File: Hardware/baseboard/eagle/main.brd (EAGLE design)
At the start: 359.1 x 113.3 mm, 182 parts, among them J1 MICROUSB-FEM, X1 JST-4POS-2X4POS, X1.2 TACH/LAP, X2 ATLAS-LTC, X2.1 MOTOR, X2.2 VRAILS+, X2.3 5V+SoC, X5 15244441

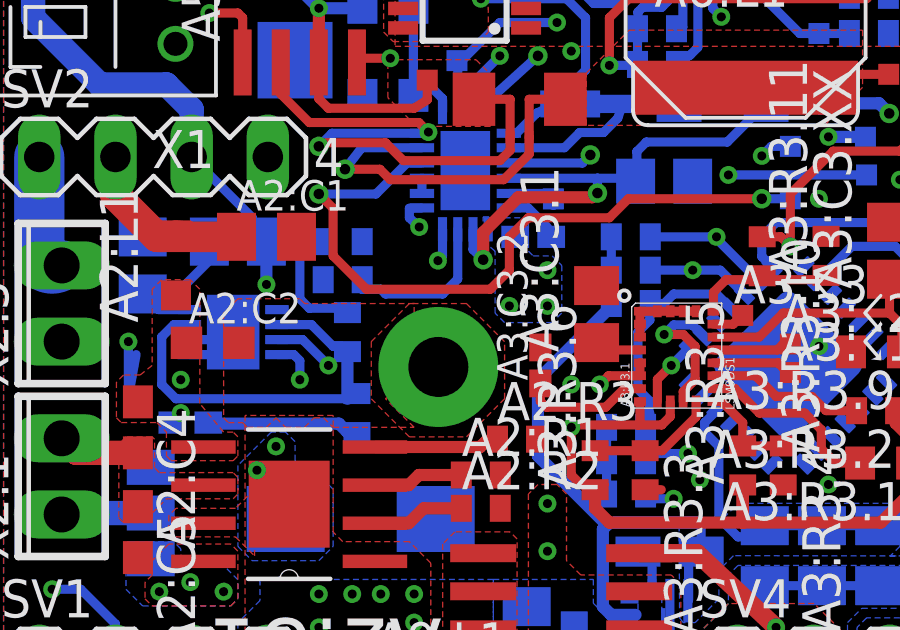
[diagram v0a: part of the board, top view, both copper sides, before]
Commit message: wip baseboard  -> layout: did some easy airwires
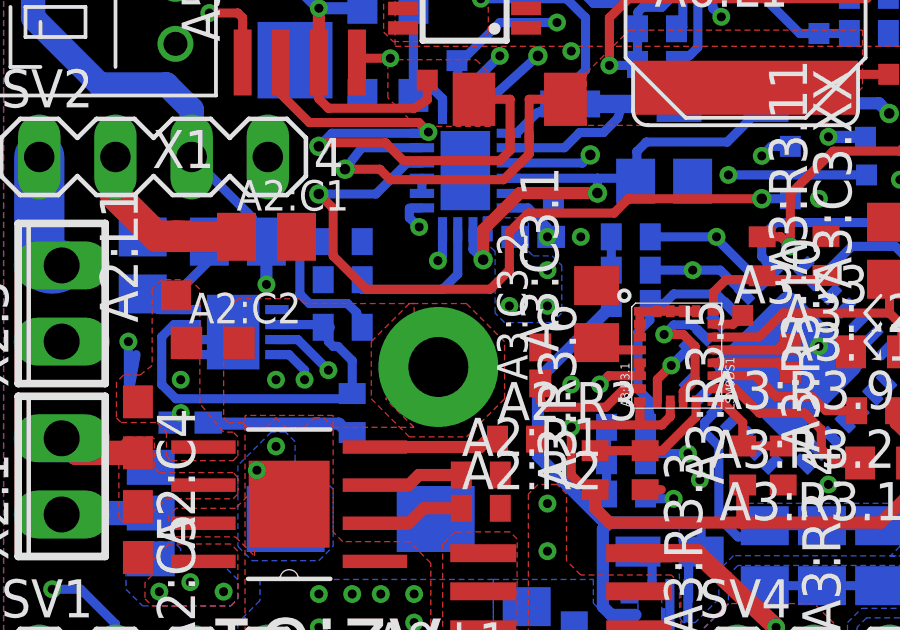
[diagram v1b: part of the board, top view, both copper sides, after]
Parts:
- moved A10:R2 0.22 mm to (17.3, 30.3), turned to 180 degrees
- moved A10:R1 0.16 mm to (17.6, 27.5)
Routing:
- net A10:HYST: track 4.38 -> 5.12 mm
- net GND: vias 40 -> 43

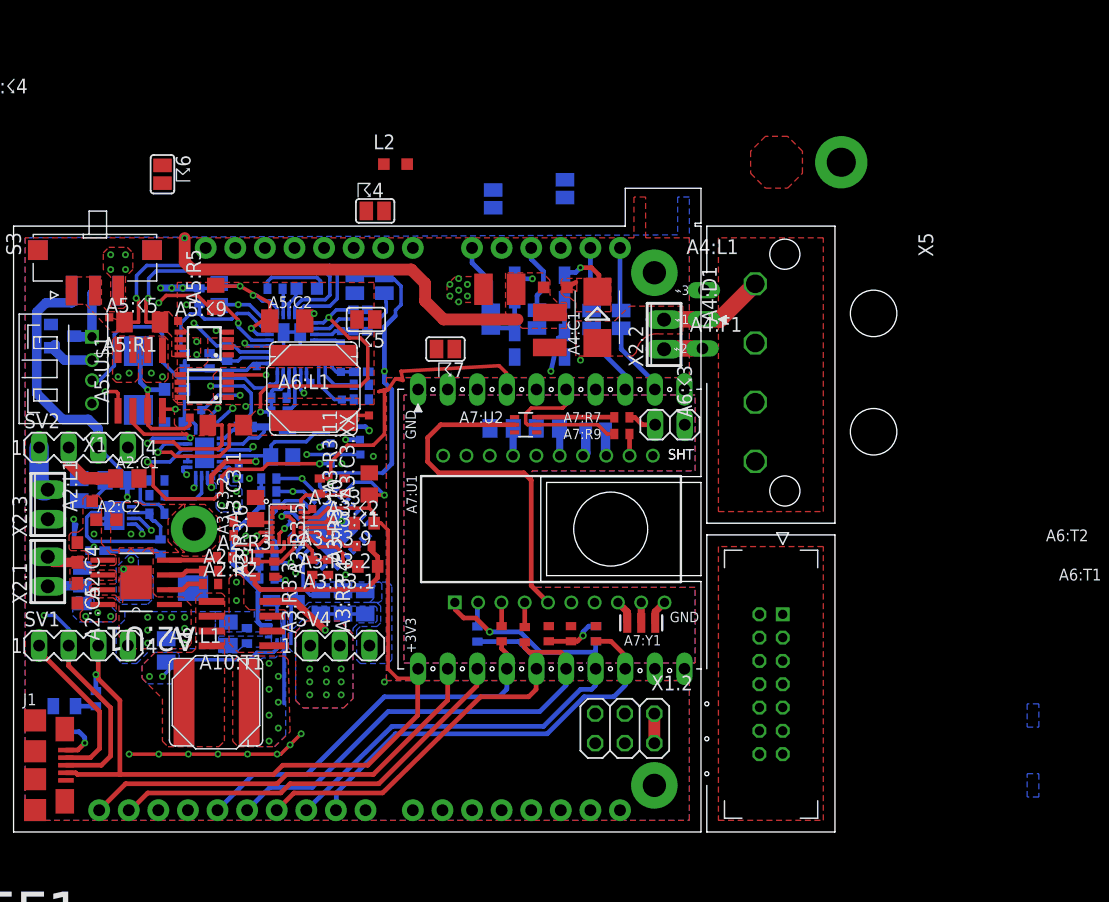
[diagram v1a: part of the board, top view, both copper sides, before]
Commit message: wip baseboard layout quicksave  + schematic    -> revised high side guard, added NAND logic  + layout    -> moved entire guard circuit on north west corner,       ideal fit acutally. Spooky how this works.    -> redo of input protection and powerlines,       make slightly more sense now
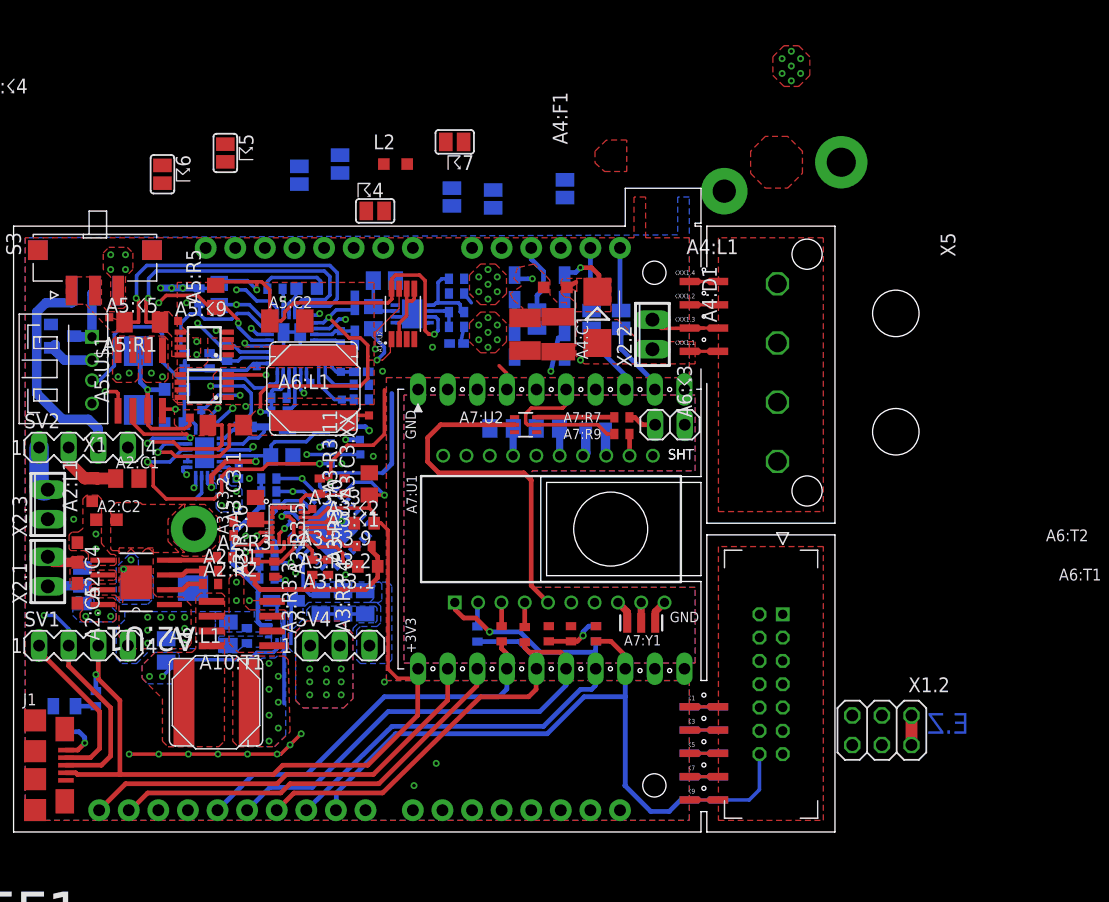
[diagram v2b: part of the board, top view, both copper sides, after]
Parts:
- removed ⌁1: SINGLEPAD40MIL-BREAK.PILOT, kitt.con:PAD40MIL.BREAK_PILOT
- removed ⌁2, ⌁3: SINGLEPAD40MIL-BREAK, kitt.con:PAD40MIL.BREAK
- added A10:U2: 2NANDSOP8, kitt.ic:SOP65P490X110-8N
- added ☇1: 1, kitt.con:CON.BUOC.BREAKPAD-P5MM
- added ☇10: 10, kitt.con:CON.BUOC.BREAKPAD-P5MM
- added ☇2: 2, kitt.con:CON.BUOC.BREAKPAD-P5MM
- added ☇3: 3, kitt.con:CON.BUOC.BREAKPAD-P5MM
- added ☇4: 4, kitt.con:CON.BUOC.BREAKPAD-P5MM
- added ☇5: 5, kitt.con:CON.BUOC.BREAKPAD-P5MM
- added ☇6: 6, kitt.con:CON.BUOC.BREAKPAD-P5MM
- added ☇7: 7, kitt.con:CON.BUOC.BREAKPAD-P5MM
- added ☇8: 8, kitt.con:CON.BUOC.BREAKPAD-P5MM
- added ☇9: 9, kitt.con:CON.BUOC.BREAKPAD-P5MM
- added ☇XX1.1: VRAILS, kitt.con:CON.BUOC.BREAKPAD-P5MM
- added ☇XX1.2, ☇XX1.3: GND, kitt.con:CON.BUOC.BREAKPAD-P5MM
- added ☇XX1.4: +5V, kitt.con:CON.BUOC.BREAKPAD-P5MM
- A6:L1: value 4.7uH -> 10uH
- A6:R2: value 120kR/1% -> 51kR/1%
- A6:R3: value 27kR/1% -> 12kR/1%
- moved A10:C1 35.6 mm to (43.0, 44.9)
- moved A10:R3 31.7 mm to (36.8, 50.3), turned to 0 degrees
- moved A10:R1 31.7 mm to (43.0, 46.4), turned to 0 degrees
- moved A10:R2 31.0 mm to (43.0, 47.6)
- moved A10:R7 31.0 mm to (43.0, 50.5)
- moved A6:C1 31.0 mm to (43.0, 49.2)
- moved A10:U1 30.9 mm to (39.2, 47.5)
- moved A10:R4 26.1 mm to (35.9, 47.1), turned to 270 degrees
- moved X1.2 22.1 mm to (79.5, 11.7)
- moved ☈5 18.7 mm to (23.2, 61.3), turned to 270 degrees
- moved ☈7 17.8 mm to (42.9, 62.2)
- moved ☈12 11.0 mm to (33.0, 60.3)
- moved ☈1 11.0 mm to (42.6, 57.5)
- moved ☈8 10.5 mm to (29.5, 59.4)
- moved A4:F1 4.42 mm to (48.9, 45.7), turned to 270 degrees
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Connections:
- removed net A10:!FAIL: A10:T1.4, A10:U1.8
- removed net A5:BIAS: A5:C4.1, A5:R11.2, A5:R12.2, A5:U1.1, A5:U1.13
- new net A10.!ACT: A10:T1.4, A10:U2.7
- new net A10:BATOK: A10:U1.8, A10:U2.2, A10:U2.5, A10:U2.6
- new net TOP.!BATOK: A10:U2.3
- new net TOP.PWRON: A10:U2.1, A5:C4.1, A5:R11.2, A5:R12.2, A5:U1.1, A5:U1.13
- net !CS1: now also X2.14, ☇10.X1
- net +3V3: now also X2.10, X2.2
- net +5V: now also ☇XX1.4.X1; no longer ⌁3.P$1
- net +9V: now also X2.1
- net A10:HYST: now also A10:U1.5
- net A10:IN-: now also A10:U1.3; no longer A10:U1.4
- net A10:REF: now also A10:U1.4; no longer A10:U1.3
- net GND: now also A10:U2.4, X2.2.2, ☇XX1.2.X1, ☇XX1.3.X1; no longer X2.2.1, ⌁2.P$1
- net MISO: now also X2.5
- net MOSI: now also X2.6
- net VCC/2: now also X2.2.1, ☇XX1.1.X1; no longer X2.2.2, ⌁1.P$1
- net VDD: now also A10:U2.8
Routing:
- net +5V: track 174.7 -> 106.7 mm
- net A10.!ACT: track 0.00 -> 41.2 mm, vias 0 -> 2
- net +18V: track 73.9 -> 41.1 mm, vias 2 -> 8
- net TOP.PWRON: track 0.00 -> 31.4 mm, vias 0 -> 2
- net A10:!FAIL: track 28.3 -> 0.00 mm, vias 2 -> 0
- net A5:BIAS: track 27.6 -> 0.00 mm, vias 2 -> 0
- net !CS1: track 35.7 -> 60.2 mm
- net VDD: track 67.8 -> 92.1 mm
- net +4.1V: track 66.8 -> 86.9 mm
- net TOP.!RST: track 28.2 -> 13.9 mm
- net GND: track 66.0 -> 51.7 mm, vias 43 -> 44
- net TOP.RRX: track 60.1 -> 45.8 mm
- net +3V3: track 84.1 -> 71.7 mm
- net A10:REF: track 13.5 -> 2.98 mm
- net VCC/2: track 9.10 -> 0.00 mm
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- added copper zone on layer 15, net +18V
- removed copper zone on layer 16, net N$26
- removed copper zone on layer 16, net N$27
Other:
- outline, holes or cut-outs redrawn
- board text added: "DOUBLE UP!"
- board text added: "E.Z"
- board text added: "TODO"
- board text added: "TODO LATR"
- board text removed: "FLIP"
- board text removed: "VRAIL"

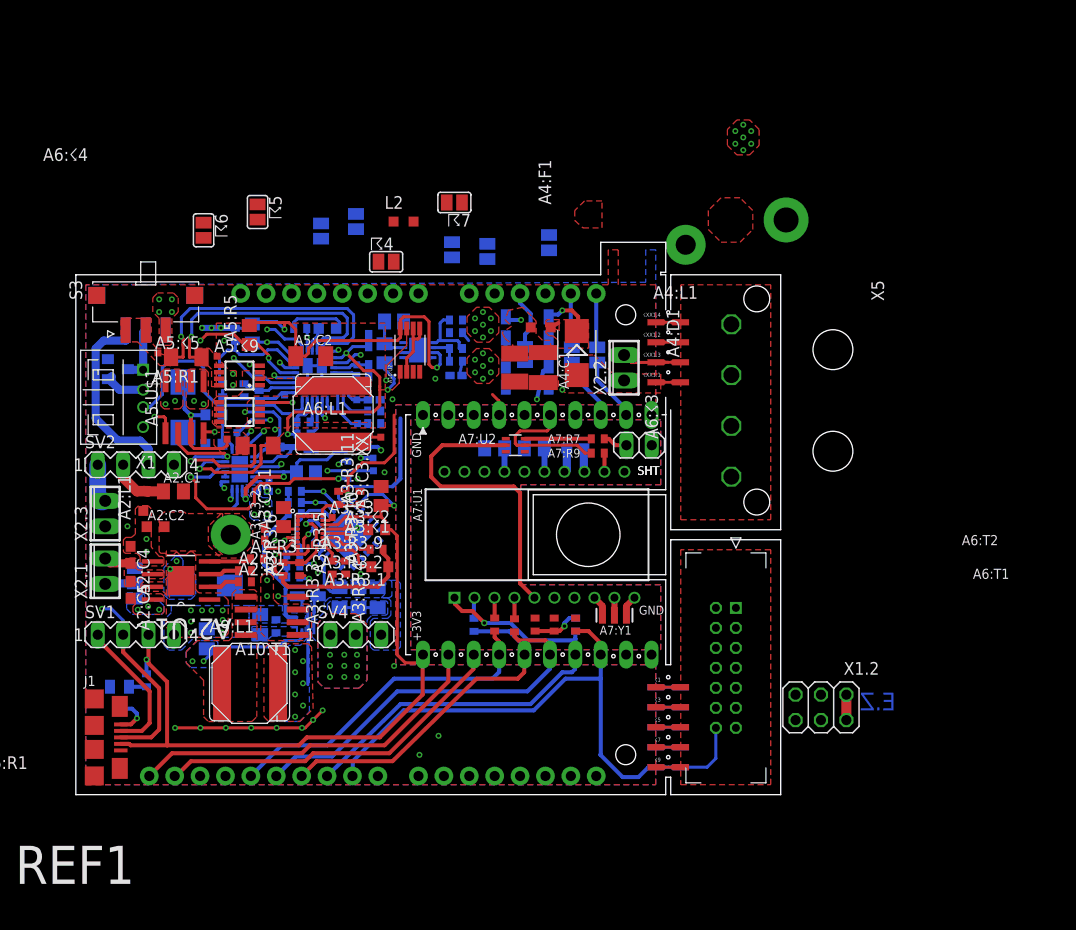
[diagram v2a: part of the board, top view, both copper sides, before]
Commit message: wip baseboard layout  + just now realized/looked up that I've had plans    initially to extend the north/south edge of the board area    which makes the jumper situation really easy  + motor is now connected via a jumper wire  + reminder that this design is still smaller    than a credit card  + pretty much finished on battery guard
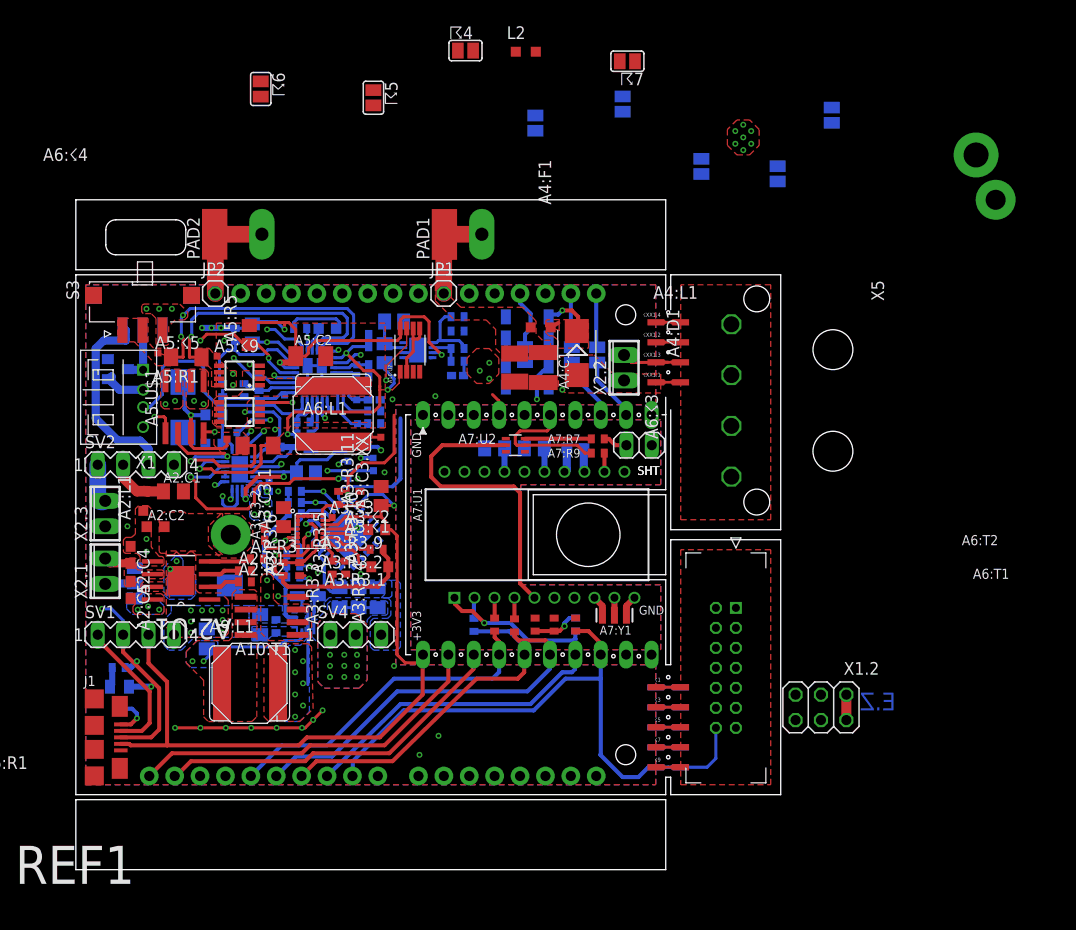
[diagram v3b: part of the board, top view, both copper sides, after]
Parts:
- added F2: (no value), fuse:SH22
- added JP1, JP2: (no value), pinhead:1X01
- added PAD1, PAD2: WIREPADSMD2,54-5,08, wirepad:SMD2,54-5,08
- moved ☈1 40.3 mm to (80.6, 71.0)
- moved ☈2 30.1 mm to (75.2, 65.1)
- moved ☈12 29.1 mm to (59.7, 72.1)
- moved ☈8 24.0 mm to (51.0, 70.2)
- moved ☈4 22.6 mm to (44.0, 77.4)
- moved ☈7 22.3 mm to (60.2, 76.4)
- moved L2 20.9 mm to (50.0, 77.3)
- moved ☈9 17.0 mm to (67.6, 65.8)
- moved ☈5 16.3 mm to (34.8, 72.7)
- moved ☈6 15.2 mm to (23.5, 73.6)
- moved R1 3.05 mm to (9.29, 15.7), turned to 0 degrees
- moved A10:R7 0.35 mm to (43.2, 50.8)
- moved S1 0.32 mm to (11.7, 51.0)
- moved S3 0.32 mm to (11.7, 51.0)
- moved A6:C1 0.22 mm to (43.2, 49.4)
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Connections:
- new net TOP.18V/PREFUSE: A4:C1.1, A4:F1.1, A4:L1.2, A4:R3.2, F2.1, JP1.1, PAD1.1
- net +18V: now also F2.2, JP2.1, PAD2.1; no longer A4:C1.1, A4:F1.1, A4:L1.2, A4:R3.2
- net +5V: now also D1.2; no longer D1.1
- net N$4: now also D1.1; no longer D1.2
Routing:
- net TOP.18V/PREFUSE: track 0.00 -> 9.68 mm
- net +4.1V: track 86.9 -> 78.9 mm
- net +18V: track 41.1 -> 47.5 mm, vias 8 -> 0
- net +5V: track 106.7 -> 103.3 mm, vias 0 -> 1
- net A8:A1: track 14.0 -> 12.5 mm
- net A6:TRACK/SS: track 3.21 -> 4.26 mm, vias 0 -> 1
- net TOP.MODE: track 14.7 -> 15.5 mm
- net GND: track 51.7 -> 52.4 mm
- net VDD: track 92.1 -> 91.3 mm
- added copper zone on layer 1, net TOP.18V/PREFUSE
- removed copper zone on layer 1, net +18V
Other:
- outline, holes or cut-outs redrawn
- board text added: "FIND ALTPART"
- board text added: "RATING!"
- board text added: "Size less than credit card by the way. Fuck me."
- board text removed: "RIPUP CORNER"

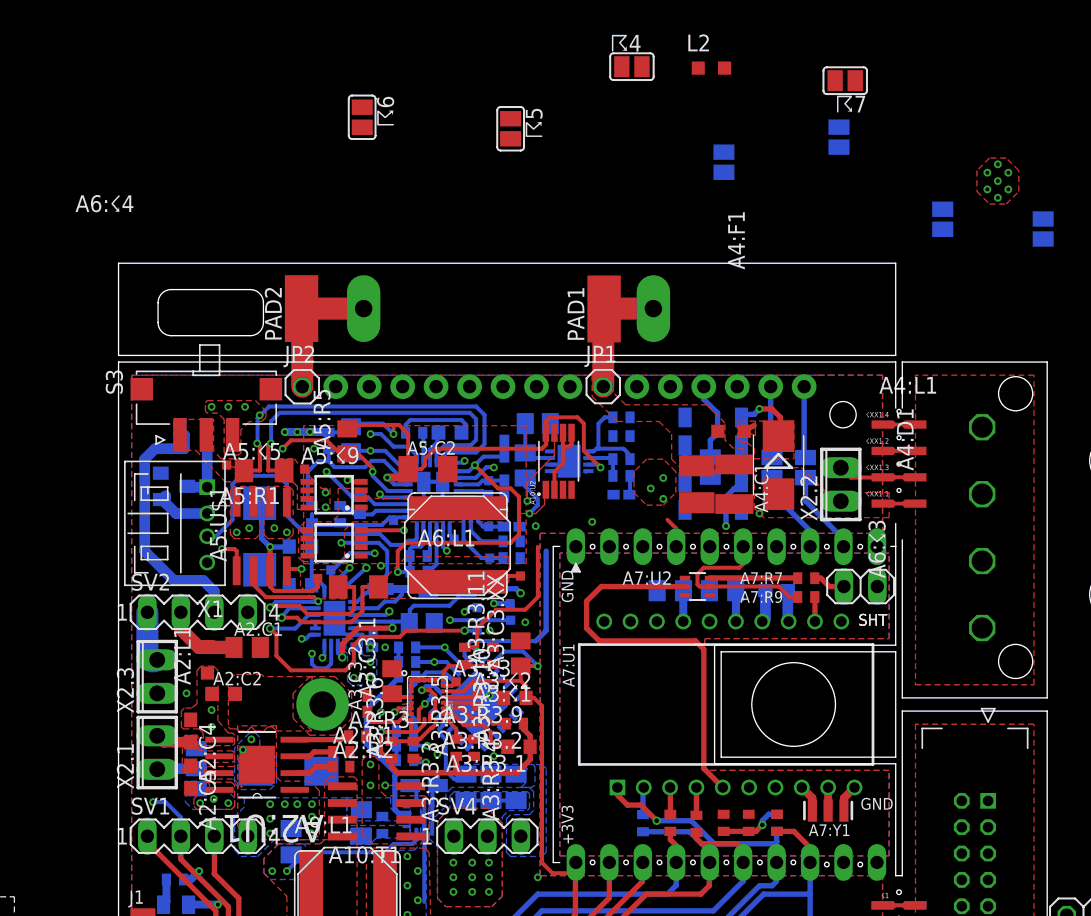
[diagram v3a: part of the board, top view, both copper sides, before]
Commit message: wip baseboard layout  + found a superiour solultion to center area on layer 3  + wire distance is effectively quater'd for all important    signals
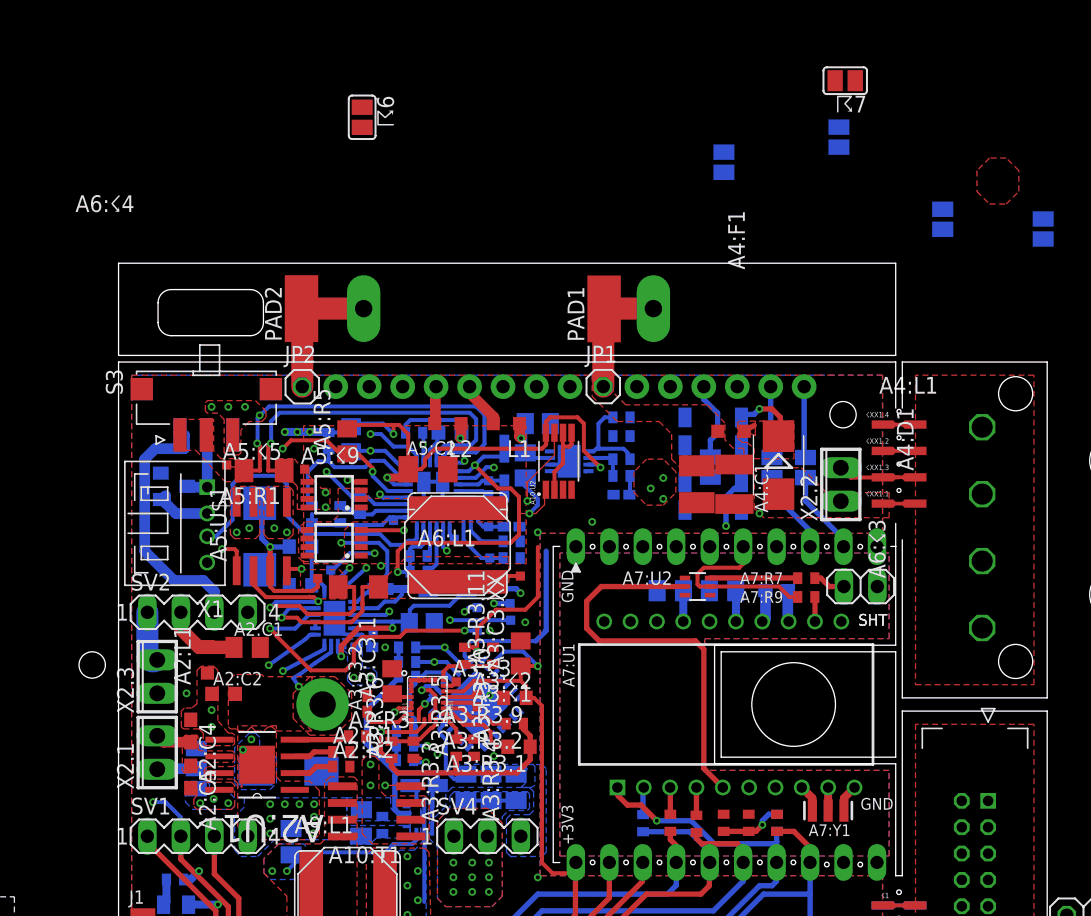
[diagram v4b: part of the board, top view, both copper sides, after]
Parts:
- removed ☈4, ☈5: (no value), jumper:SJ
- added L1: BEAD/0R/⎵, rcl:L2012C
- moved L2 33.6 mm to (30.0, 50.3), turned to 180 degrees
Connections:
- removed net N$19: ☈5.1, ☈6.1
- net +3V3: now also L2.1
- net +5V: now also L1.1; no longer ☈4.1
- net UNO.3V3: now also L2.2; no longer ☈5.2
- net UNO.5V: now also L1.2; no longer ☈4.2
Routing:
- net +5V: track 103.3 -> 52.5 mm, vias 1 -> 2
- net TOP.MODE: track 15.5 -> 29.2 mm
- net VDD: track 91.3 -> 80.7 mm
- net TOP.FREQ: track 16.6 -> 23.9 mm
- net A6:TRACK/SS: track 4.26 -> 7.98 mm
- net UNO.5V: track 0.00 -> 3.59 mm
- net +3V3: track 71.7 -> 74.6 mm, vias 4 -> 5
- net UNO.3V3: track 0.08 -> 2.88 mm
- net SYSTWI.SDA: track 145.9 -> 147.2 mm
- net SYSTWI.SCL: track 145.8 -> 146.8 mm
- net TOP.RUN: track 23.8 -> 22.9 mm
- net GND: vias 44 -> 42
- net DDC.CLN/VIN: vias 5 -> 4
- removed copper zone on layer 15, net +18V
